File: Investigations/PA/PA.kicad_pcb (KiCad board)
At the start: 2 copper layers, 88.9 x 43.2 mm, 21 parts, among them J1 CLK, J2 OUT, J3 0022232041, Q1 BS170, Q2 BS170, T1 BN43-202, U1 SN74LVC2G86DCTR

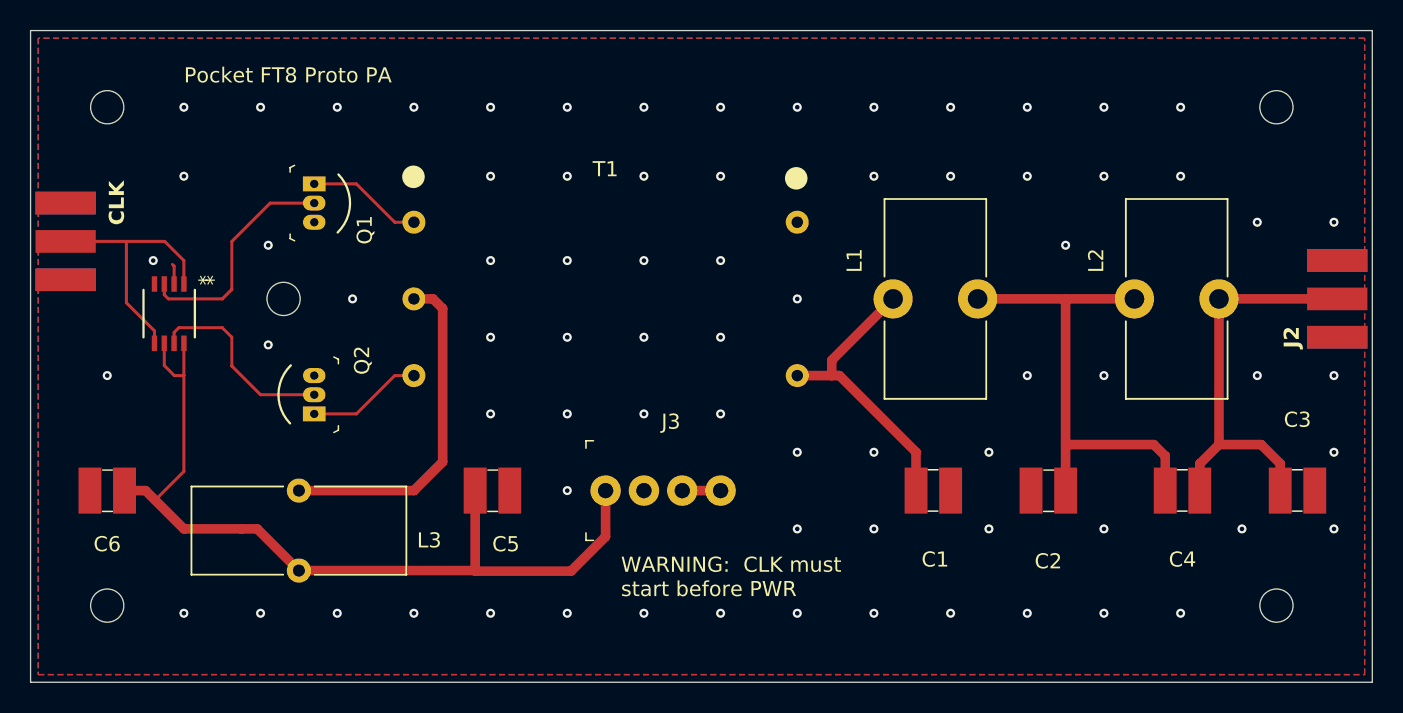
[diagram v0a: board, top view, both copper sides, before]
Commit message: PA Proto submitted to PCBWay
First PA Proto uses XOR to generate differentials, (2) BS170 finals, 5Vcc, and Chebyshev LP filter on a 2-Layer Board.
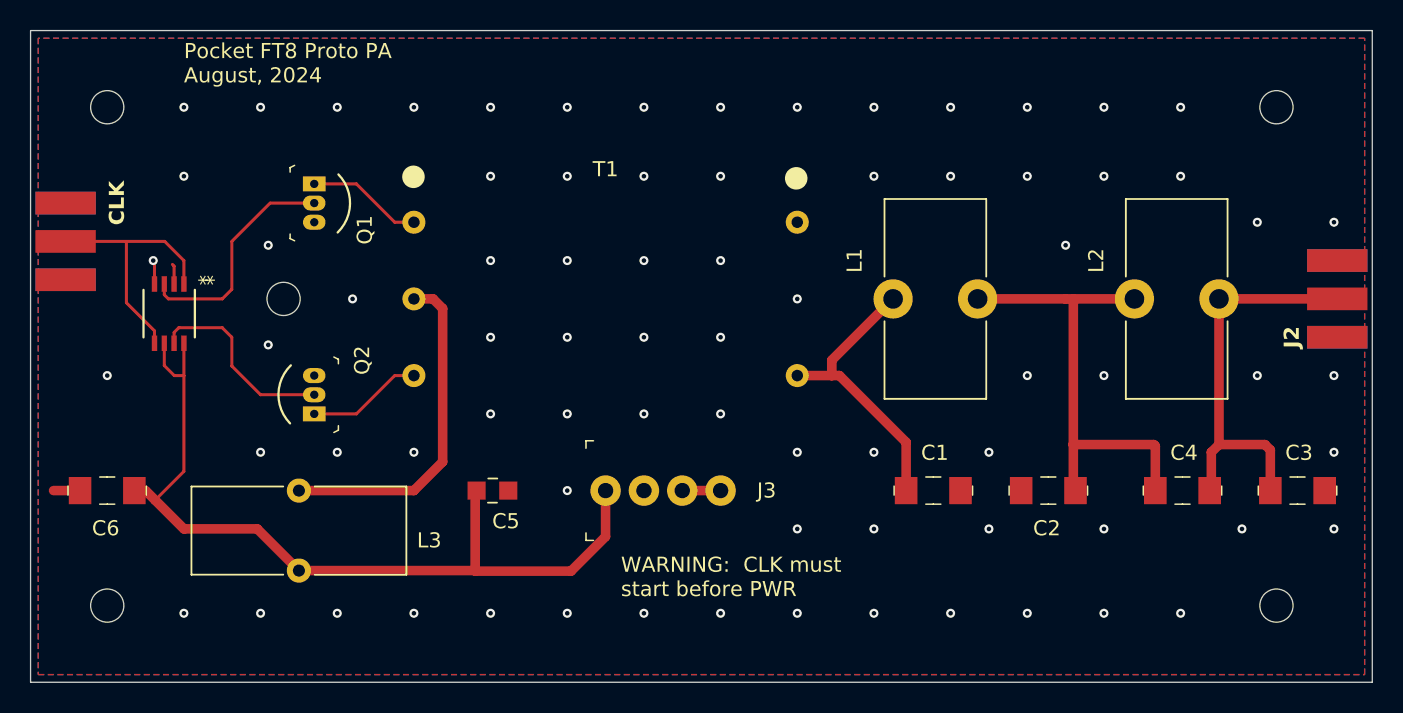
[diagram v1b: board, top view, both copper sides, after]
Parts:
- C1, C2, C3, C4, C6: footprint digikey-footprints:1210 -> digikey-footprints:1206
- C5: footprint digikey-footprints:1210 -> digikey-footprints:0805
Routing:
- net GND: track 3.89 -> 7.23 mm, vias 74 -> 77
- net Net-(C2-Pad1): track 32.3 -> 31.5 mm
- net +5V: track 57.7 -> 57.0 mm
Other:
- board text added: "Pocket FT8 Proto PA August, 2024"
- board text removed: "Pocket FT8 Proto PA"
